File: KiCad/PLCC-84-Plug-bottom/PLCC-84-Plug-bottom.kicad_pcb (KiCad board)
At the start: 2 copper layers, 33 x 33 mm, 5 parts, among them J1 Conn_01x01, J2 Conn_01x01, J3 Conn_01x01, J4 Conn_01x01, U1 Dummy_symbol

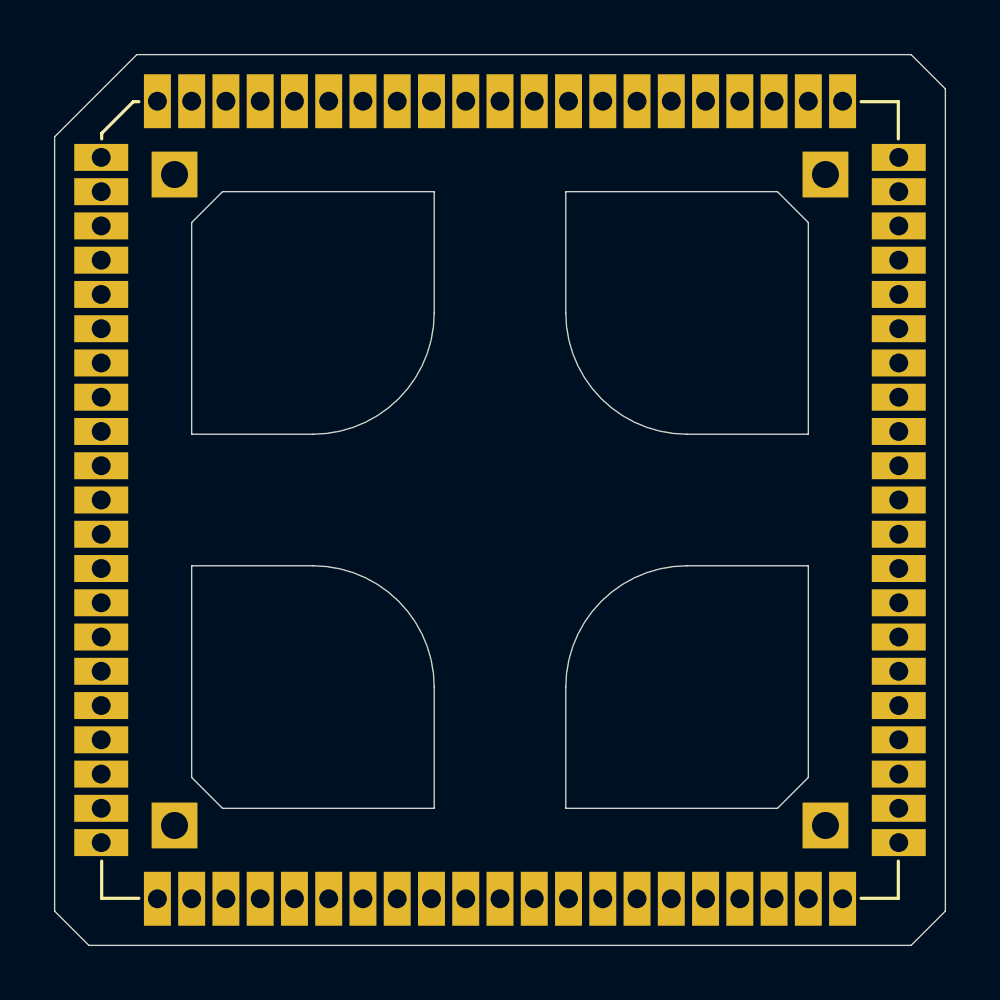
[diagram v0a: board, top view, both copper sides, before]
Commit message: made a new revision 1B with modified size
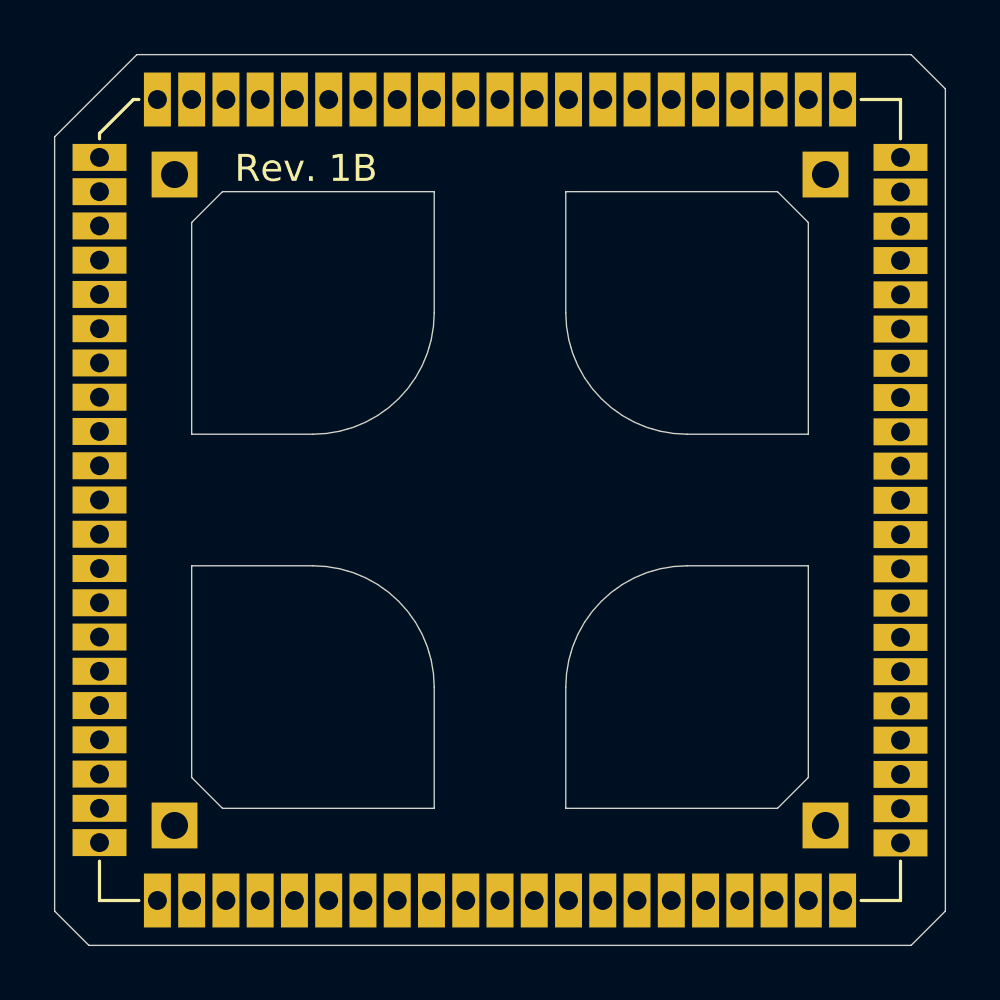
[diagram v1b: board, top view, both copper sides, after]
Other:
- board text added: "Rev. 1B"

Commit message: small fix SolderMaskClearance setting
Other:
- rule pad_to_mask_clearance: 0.05 -> 0.0
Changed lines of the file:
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@@
     (pad_size 1 1)
     (pad_drill 0.5)
-    (pad_to_mask_clearance 0.05)
+    (pad_to_mask_clearance 0.0)
     (aux_axis_origin 0 0)
     (grid_origin 76.2 63.5)

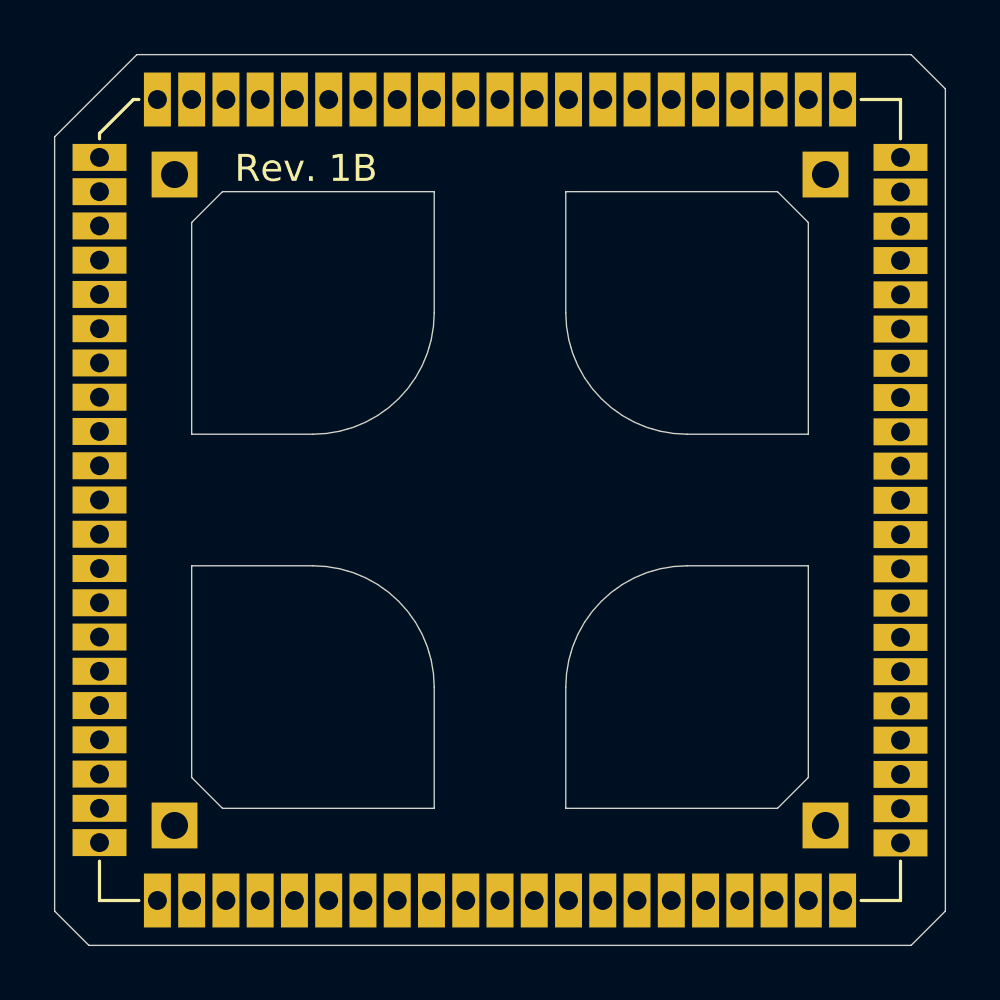
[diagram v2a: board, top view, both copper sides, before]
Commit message: Updated dimensions and openframe to support level shifters on underside, Rev 1C
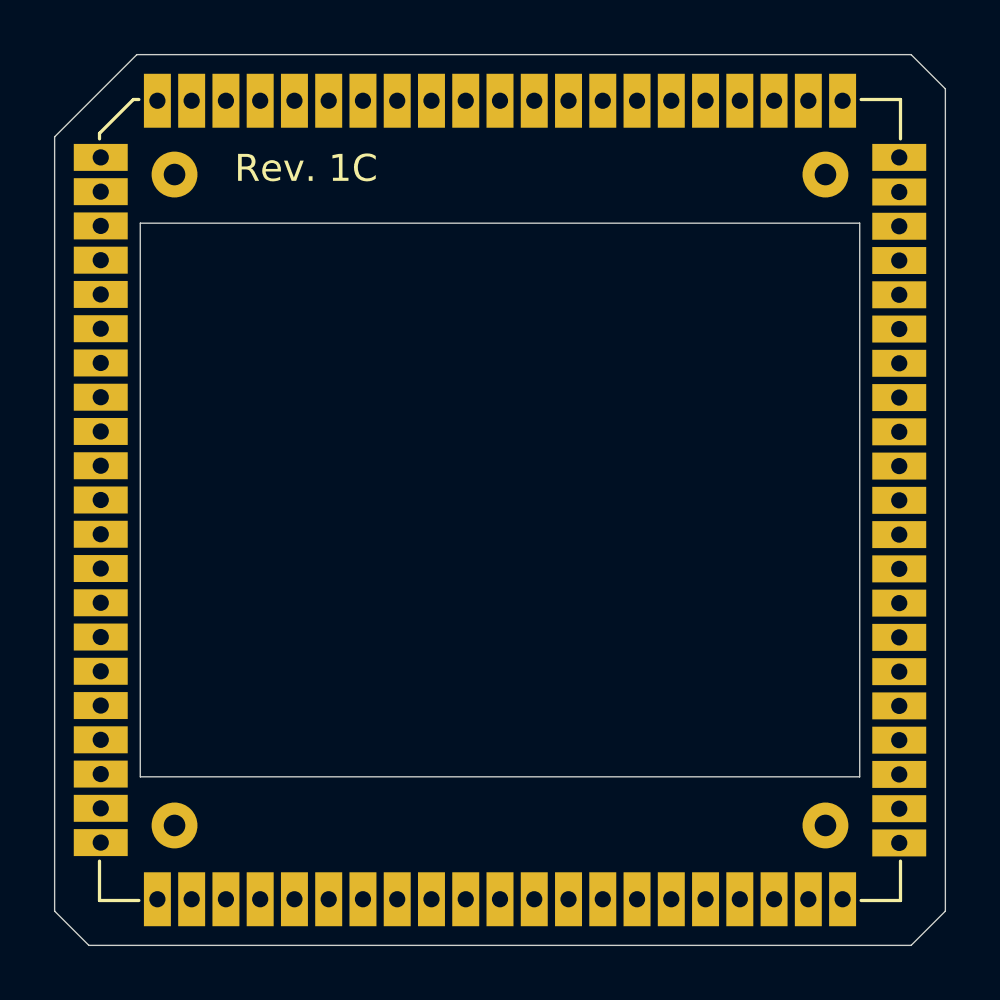
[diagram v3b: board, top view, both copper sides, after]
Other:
- outline, holes or cut-outs redrawn
- rule pad_to_mask_clearance: 0.0 -> 0
- board text added: "Rev. 1C"
- board text removed: "Rev. 1B"
